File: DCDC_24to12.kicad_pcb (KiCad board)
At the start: 2 copper layers, 69.8 x 29.8 mm, 28 parts, among them J1 Power_IN, J2 Power_OUT, U1 BD9F800MUX-ZE2

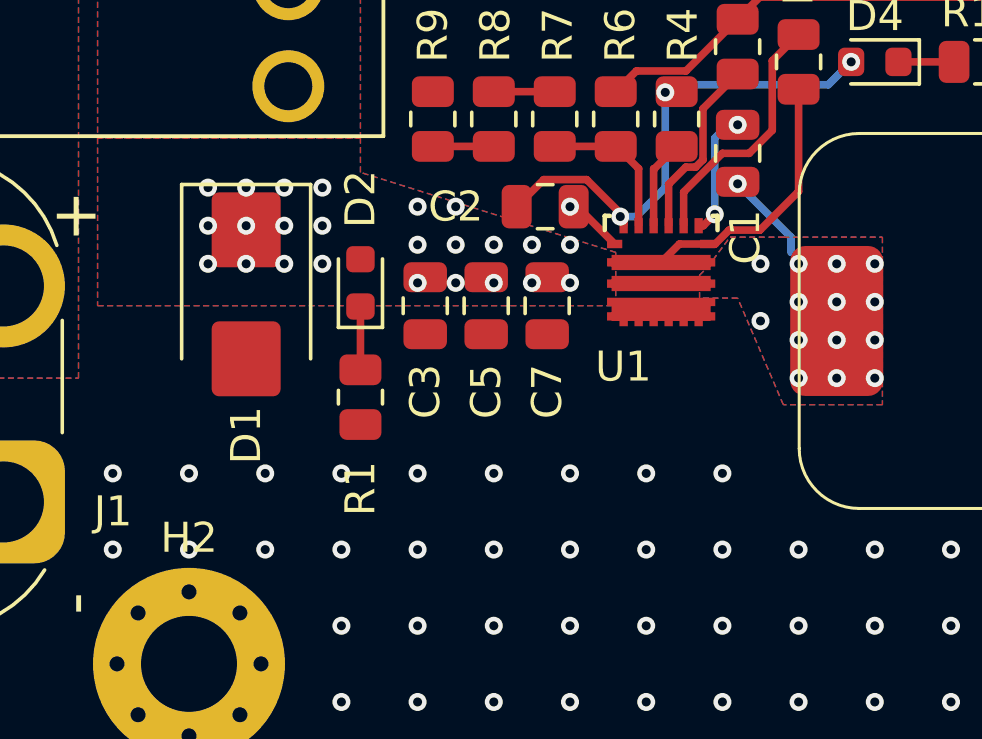
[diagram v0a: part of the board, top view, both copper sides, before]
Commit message: ビアへの配線を明示的にした
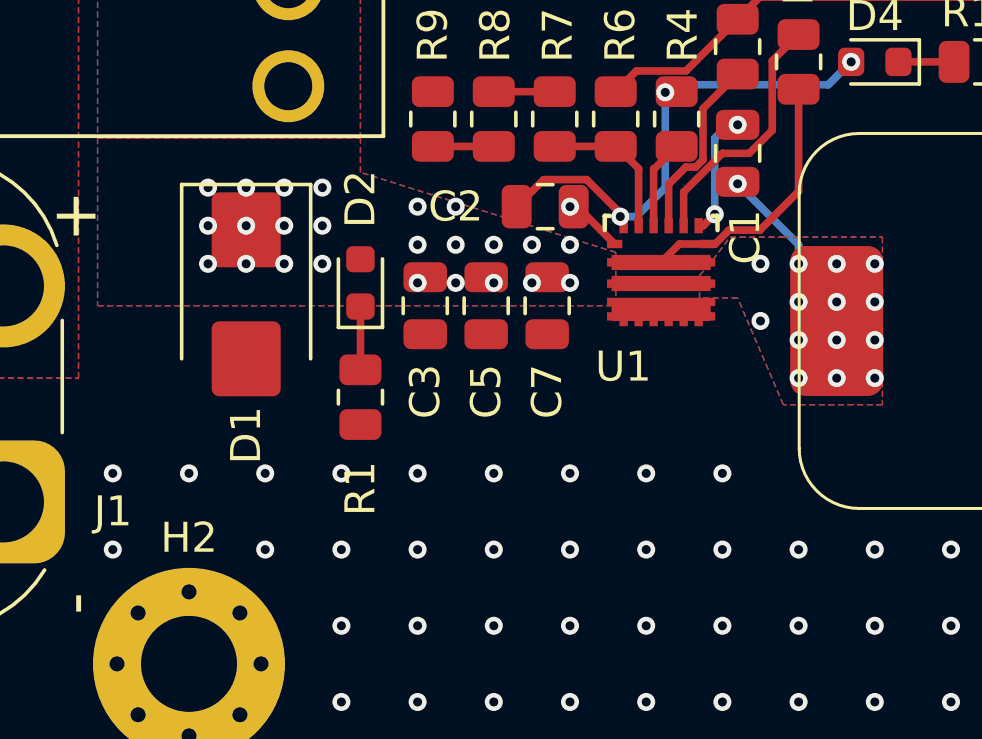
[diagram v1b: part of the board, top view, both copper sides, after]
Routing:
- net GND: vias 87 -> 86
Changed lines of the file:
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@@
 		(tags "resistor")
 		(property "Reference" "R10"
-			(at 0 -1.65 360)
+			(at 0 -1.65 0)
 			(layer "F.SilkS")
 			(effects
@@
 		)
 		(property "Value" "1k"
-			(at 0 1.65 360)
+			(at 0 1.65 0)
 			(layer "F.Fab")
 			(effects
@@
 		)
 		(fp_text user "${REFERENCE}"
-			(at 0 0 360)
+			(at 0 0 0)
 			(layer "F.Fab")
 			(effects
@@
 		(tags "capacitor")
 		(property "Reference" "C2"
-			(at 2.981999 0 360)
+			(at 2.981999 0 0)
 			(layer "F.SilkS")
 			(effects
@@
 		)
 		(property "Value" "2.2uF"
-			(at -0.254 1.651 360)
+			(at -0.254 1.651 0)
 			(layer "F.Fab")
 			(effects
@@
 		)
 		(fp_text user "${REFERENCE}"
-			(at 0 0 360)
+			(at 0 0 0)
 			(layer "F.Fab")
 			(effects
@@
 		(tags "LED")
 		(property "Reference" "D4"
-			(at 0 1.524 360)
+			(at 0 1.524 0)
 			(layer "F.SilkS")
 			(effects
@@
 		)
 		(property "Value" "LED"
-			(at 0 1.43 360)
+			(at 0 1.43 0)
 			(layer "F.Fab")
 			(effects
@@
 		)
 		(fp_text user "${REFERENCE}"
-			(at 0 0 360)
+			(at 0 0 0)
 			(layer "F.Fab")
 			(effects
@@
 		(tags "LED")
 		(property "Reference" "D3"
-			(at -2.3875 0 360)
+			(at -2.3875 0 0)
 			(layer "F.SilkS")
 			(effects
@@
 		)
 		(property "Value" "LED"
-			(at 0 1.43 360)
+			(at 0 1.43 0)
 			(layer "F.Fab")
 			(effects
@@
 		)
 		(fp_text user "${REFERENCE}"
-			(at 0 0 360)
+			(at 0 0 0)
 			(layer "F.Fab")
 			(effects
@@
 		)
 		(property "Value" "Power_OUT"
-			(at -3.6 4 360)
+			(at -3.6 4 0)
 			(layer "F.Fab")
 			(effects
@@
 		)
 		(fp_text user "+"
-			(at -9.5 2.5 360)
+			(at -9.5 2.5 0)
 			(layer "F.SilkS")
 			(effects
@@
 		)
 		(fp_text user "-"
-			(at 2.8 2.5 360)
+			(at 2.8 2.5 0)
 			(layer "F.SilkS")
 			(effects
@@
 		)
 		(fp_text user "${REFERENCE}"
-			(at -3.6 -3.6 360)
+			(at -3.6 -3.6 0)
 			(layer "F.Fab")
 			(effects
@@
 		(tags "resistor")
 		(property "Reference" "R2"
-			(at 2.8175 0 360)
+			(at 2.8175 0 0)
 			(layer "F.SilkS")
 			(effects
@@
 		)
 		(property "Value" "10k"
-			(at 0 1.65 360)
+			(at 0 1.65 0)
 			(layer "F.Fab")
 			(effects
@@
 		)
 		(fp_text user "${REFERENCE}"
-			(at 0 0 360)
+			(at 0 0 0)
 			(layer "F.Fab")
 			(effects
@@
 		(at 82.935 46.355 180)
 		(property "Reference" "F1"
-			(at -11.68 2.54 360)
+			(at -11.68 2.54 0)
 			(layer "F.SilkS")
 			(effects
@@
 		)
 		(property "Value" "10A"
-			(at -3.175 4.445 360)
+			(at -3.175 4.445 0)
 			(layer "F.Fab")
 			(effects
@@
 		)
 		(property "Footprint" "FUSE_3557:FUSE_3557-2"
-			(at 0 0 360)
+			(at 0 0 0)
 			(layer "F.Fab")
 			(hide yes)
@@
 		)
 		(property "Datasheet" ""
-			(at 0 0 360)
+			(at 0 0 0)
 			(layer "F.Fab")
 			(hide yes)
@@
 		)
 		(property "Description" "Fuse, small symbol"
-			(at 0 0 360)
+			(at 0 0 0)
 			(layer "F.Fab")
 			(hide yes)
@@
 				(font
 					(size 0.5 0.5)
+					(thickness 0.15)
 				)
 			)
@@
 	)
 	(via
-		(at 86.36 63.5)
-		(size 0.6)
-		(drill 0.3)
-		(layers "F.Cu" "B.Cu")
-		(free yes)
-		(net 1)
-	)
-	(via
 		(at 129.54 68.58)
 		(size 0.6)
@@
 	)
 	(segment
-		(start 106.426 53.086)
-		(end 106.426 53.594)
+		(start 106.68 53.34)
+		(end 106.68 53.975)
 		(width 0.254)
 		(layer "B.Cu")
@@
 	(segment
 		(start 104.648 51.308)
-		(end 106.426 53.086)
+		(end 106.68 53.34)
 		(width 0.254)
 		(layer "B.Cu")

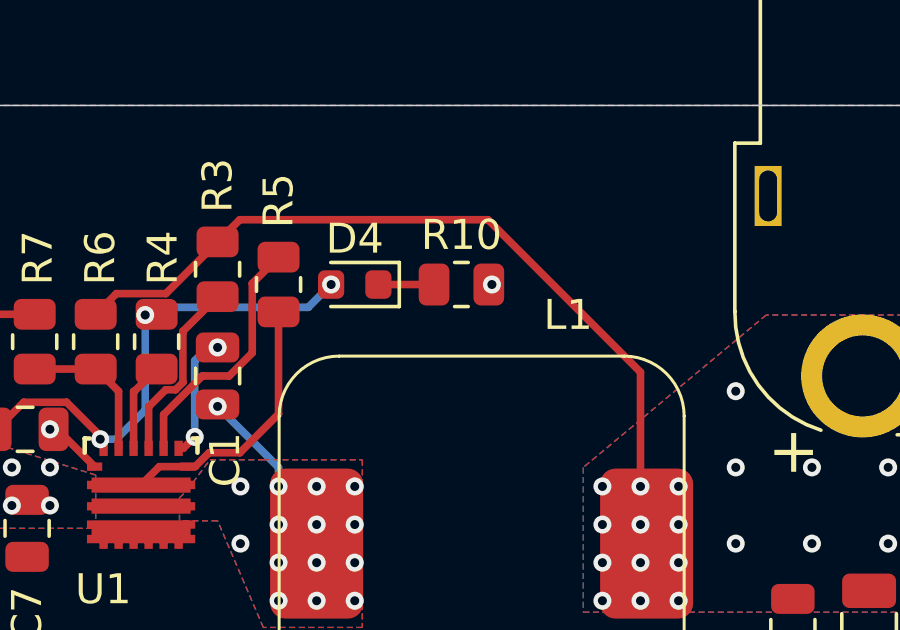
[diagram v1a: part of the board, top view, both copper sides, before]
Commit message: インダクタ上のビアとキープアウトを改善
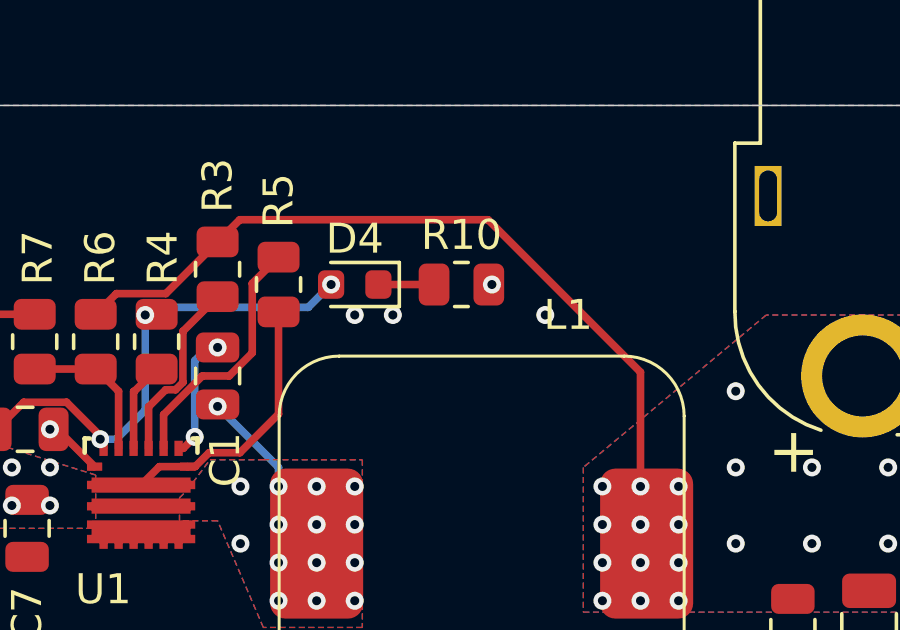
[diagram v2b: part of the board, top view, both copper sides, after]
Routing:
- net GND: vias 86 -> 89
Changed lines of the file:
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@@
+	)
+	(via
+		(at 115.57 48.26)
+		(size 0.6)
+		(drill 0.3)
+		(layers "F.Cu" "B.Cu")
+		(free yes)
+		(net 1)
 	)
 	(via
@@
 	)
 	(via
+		(at 109.22 48.26)
+		(size 0.6)
+		(drill 0.3)
+		(layers "F.Cu" "B.Cu")
+		(free yes)
+		(net 1)
+	)
+	(via
 		(at 83.82 63.5)
 		(size 0.6)
@@
 	(via
 		(at 137.16 55.88)
+		(size 0.6)
+		(drill 0.3)
+		(layers "F.Cu" "B.Cu")
+		(free yes)
+		(net 1)
+	)
+	(via
+		(at 110.49 48.26)
 		(size 0.6)
 		(drill 0.3)
@@
 		(polygon
 			(pts
-				(xy 109.982 48.895) (xy 109.982 62.992) (xy 116.586 62.992) (xy 116.586 48.895)
+				(xy 109.982 49.022) (xy 109.982 62.992) (xy 116.586 62.992) (xy 116.586 49.022)
 			)
 		)

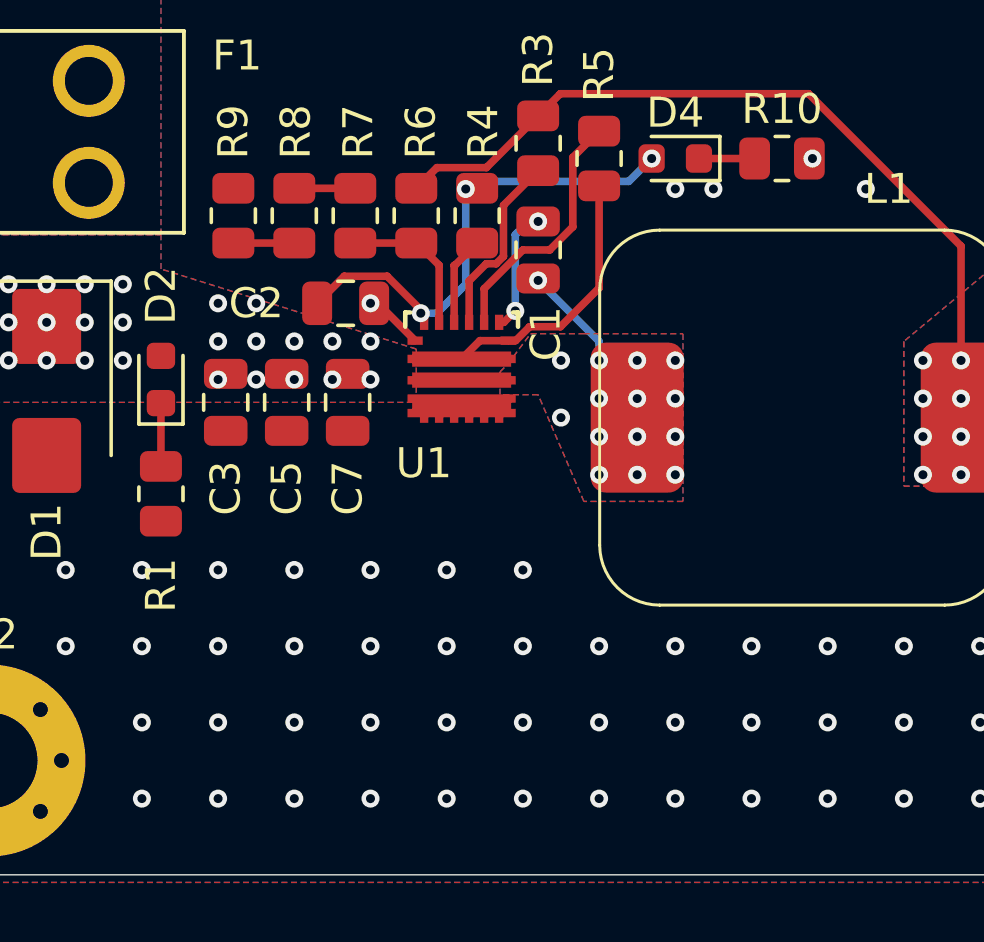
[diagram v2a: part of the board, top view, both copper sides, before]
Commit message: FB抵抗のGNDビア追加
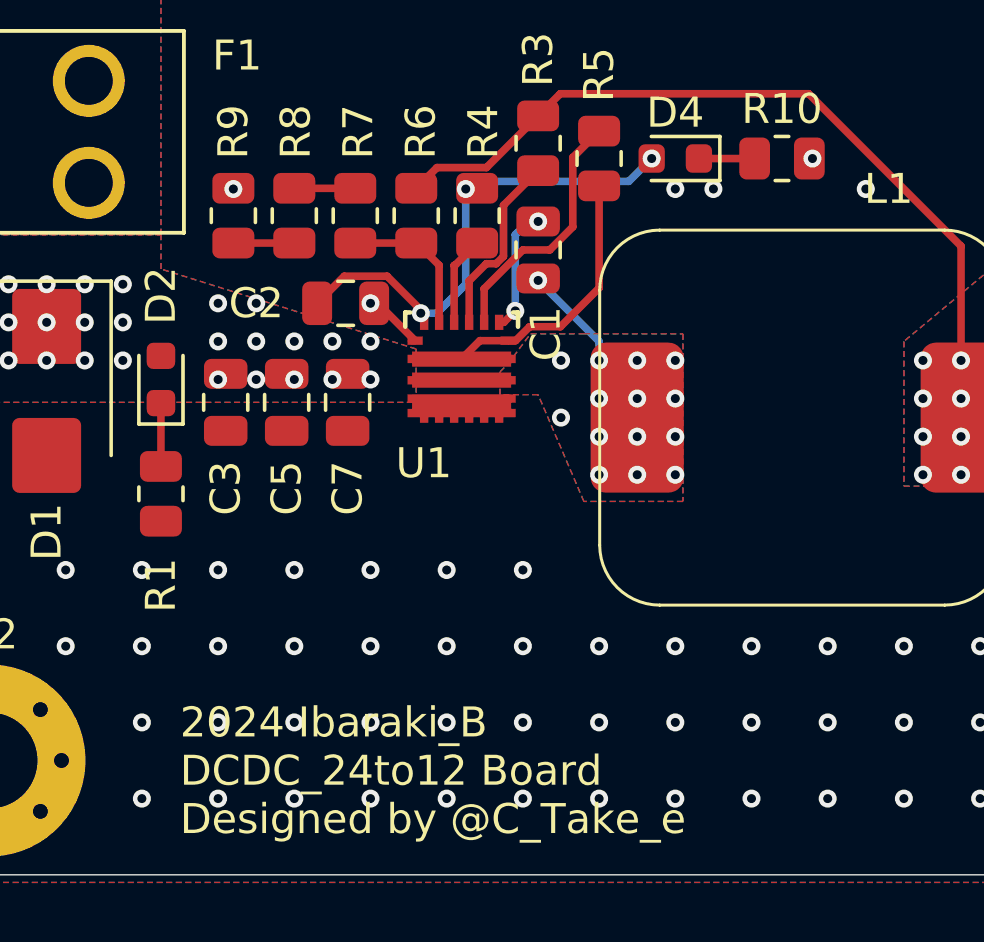
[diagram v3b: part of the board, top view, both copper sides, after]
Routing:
- net GND: vias 89 -> 90
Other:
- board text added: "2024 Ibaraki_B DCDC_24to12 Board Designed by @C_Take_e"
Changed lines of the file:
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@@
 		(layer "Edge.Cuts")
+	)
+	(gr_text "2024 Ibaraki_B\nDCDC_24to12 Board\nDesigned by @C_Take_e"
+		(at 92.71 69.85 0)
+		(layer "F.SilkS")
+		(effects
+			(font
+				(size 1 1)
+				(thickness 0.1)
+			)
+			(justify left bottom)
+		)
 	)
 	(gr_text "J2"
@@
 		(net 1)
 	)
+	(via
+		(at 94.488 48.26)
+		(size 0.6)
+		(drill 0.3)
+		(layers "F.Cu" "B.Cu")
+		(net 1)
+	)

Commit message: 配置変更案 詳細未設定
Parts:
- moved R2 31.0 mm to (101.9, 44.2), turned to 180 degrees
- moved D3 30.9 mm to (102.4, 42.2)
- moved J2 27.0 mm to (112.6, 67.6), turned to 180 degrees
- moved H1 23.2 mm to (136.5, 43.7)
- moved R1 15.2 mm to (97.4, 44.2), turned to 180 degrees
- moved D2 13.5 mm to (97.3, 42.2), turned to 180 degrees
- moved C4 11.7 mm to (115.6, 63.5), turned to 180 degrees
- moved C6 8.57 mm to (115.6, 61.0), turned to 180 degrees
- moved H2 8.32 mm to (79.2, 71.6)
- moved R10 6.15 mm to (107.6, 43.9), turned to 180 degrees
- moved D4 5.38 mm to (107.4, 42.2)
- moved L1 4.23 mm to (110.2, 52.3)
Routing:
- net +12V: track 25.4 -> 34.7 mm, vias 19 -> 38
- net +BATT: track 8.97 -> 16.8 mm
- net GND: track 2.73 -> 4.82 mm, vias 90 -> 78
- net VREG: track 16.4 -> 17.8 mm
- net SW: track 3.51 -> 2.35 mm, vias 15 -> 17
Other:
- board outline removed

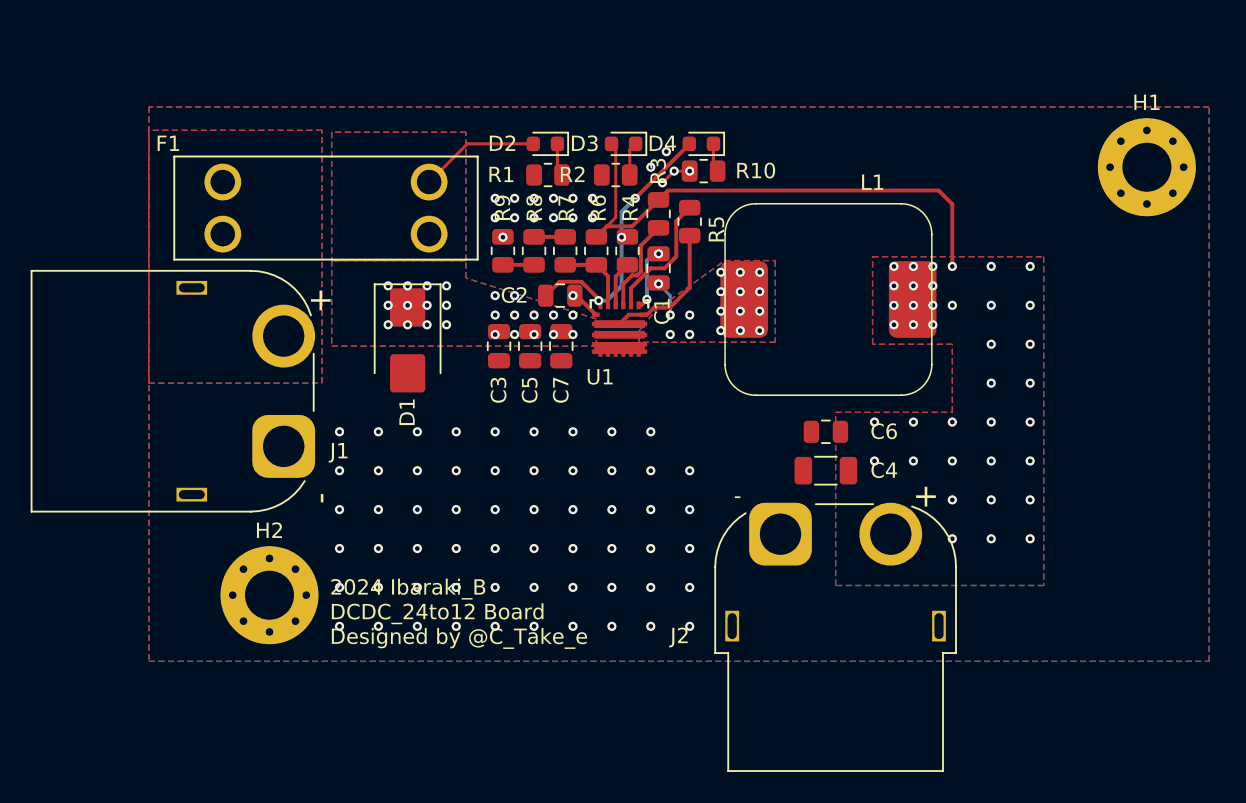
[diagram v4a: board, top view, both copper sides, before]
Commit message: 穴消したりいろいろ修正したり
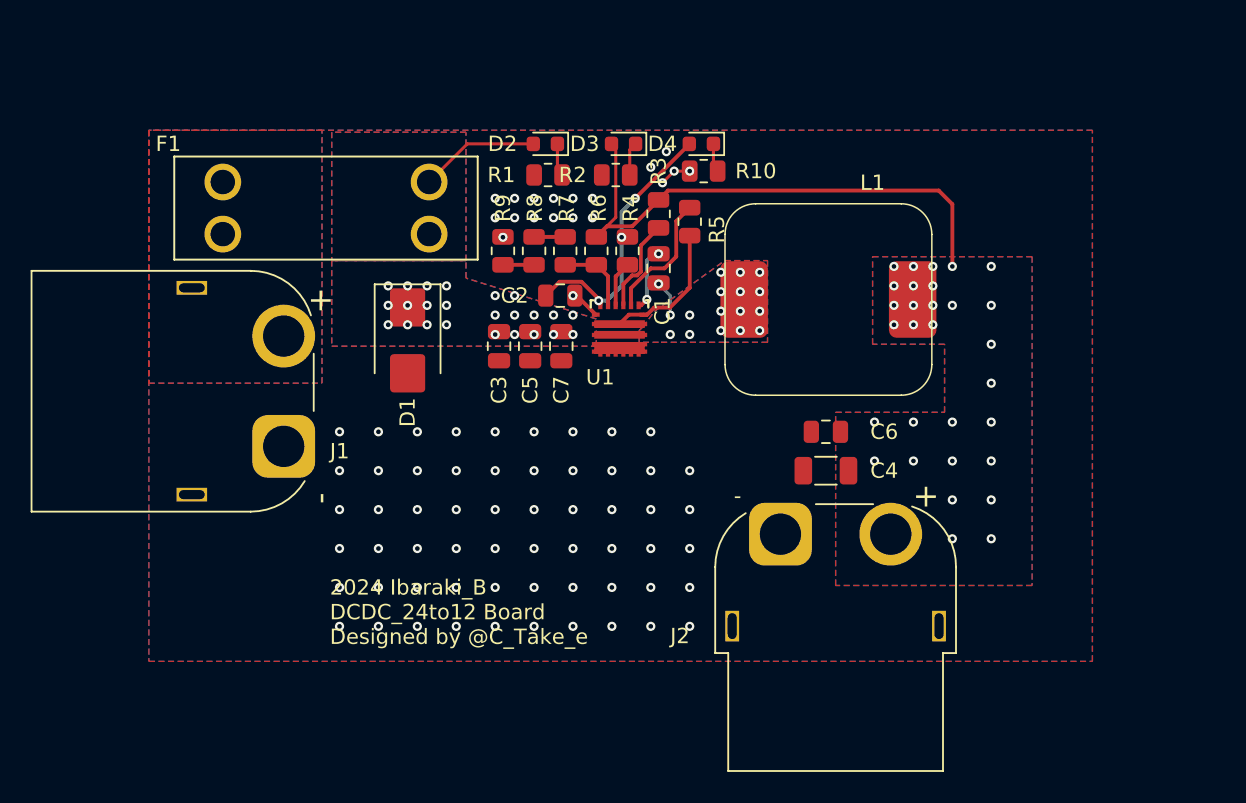
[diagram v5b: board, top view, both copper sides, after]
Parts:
- removed H1, H2: MountingHole, MountingHole:MountingHole_3.2mm_M3_Pad_Via
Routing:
- net +12V: vias 38 -> 30
